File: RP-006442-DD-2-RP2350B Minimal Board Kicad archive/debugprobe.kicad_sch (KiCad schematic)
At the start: 39 parts, among them J4 Conn_01x03, J5 USB_C_Receptacle_USB2.0_16P, SW3 SW_Push, SW4 SW_Push, U5 W25Q128JVS, U6 NCP1117-3.3_SOT223, U7 RP2350_60QFN, Y2 ABM8-272-T3

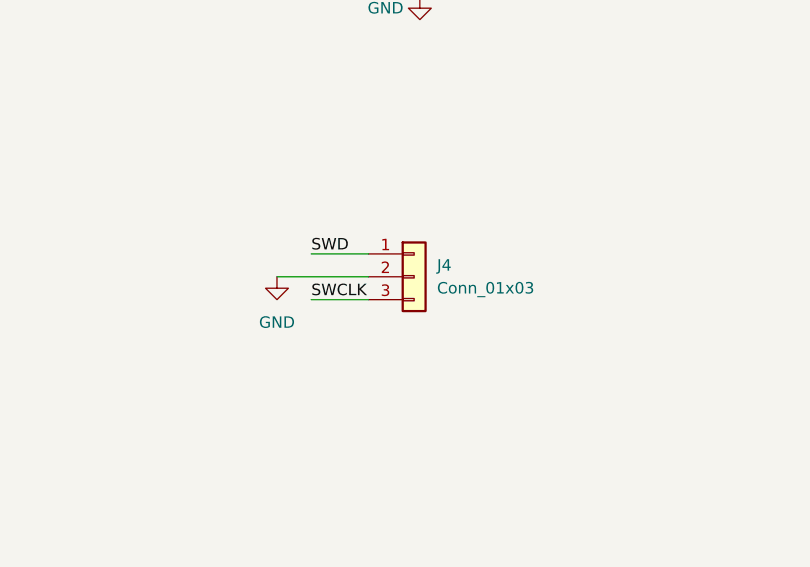
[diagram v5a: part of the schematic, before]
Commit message: Update to schematic and pcb
Changed ht16k33 package from 28SOP to 24SSOP

Placed pcb footprints
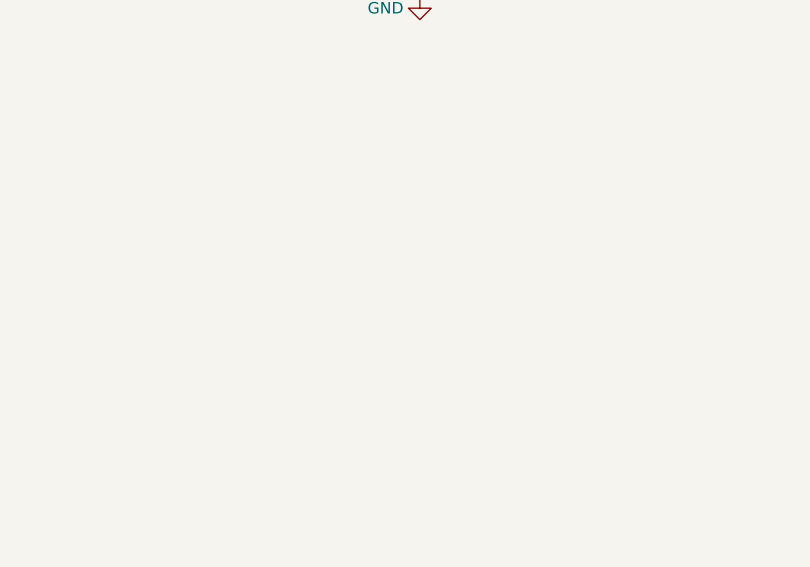
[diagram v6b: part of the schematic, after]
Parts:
- removed J4: Conn_01x03, Connector_PinHeader_2.54mm:PinHeader_1x03_P2.54mm_Vertical, symbol Connector_Generic:Conn_01x03
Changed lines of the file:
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@@
 	(wire
 		(pts
-			(xy 292.1 182.88) (xy 298.45 182.88)
-		)
-		(stroke
-			(width 0)
-			(type default)
-		)
-	)
-	(wire
-		(pts
 			(xy 118.11 49.53) (xy 118.11 50.8)
 		)
@@
 	(wire
 		(pts
-			(xy 292.1 177.8) (xy 298.45 177.8)
-		)
-		(stroke
-			(width 0)
-			(type default)
-		)
-	)
-	(wire
-		(pts
 			(xy 151.13 167.64) (xy 172.72 167.64)
 		)
@@
 	(wire
 		(pts
-			(xy 288.29 180.34) (xy 298.45 180.34)
-		)
-		(stroke
-			(width 0)
-			(type default)
-		)
-	)
-	(wire
-		(pts
 			(xy 236.22 149.86) (xy 251.46 149.86)
 		)
@@
 		)
 	)
-	(label "SWD"
-		(at 292.1 177.8 0)
-		(effects
-			(font
-				(size 1.27 1.27)
-			)
-			(justify left bottom)
-		)
-	)
 	(label "GPIO5"
 		(at 251.46 127 180)
@@
 		)
 	)
-	(label "SWCLK"
-		(at 292.1 182.88 0)
-		(effects
-			(font
-				(size 1.27 1.27)
-			)
-			(justify left bottom)
-		)
-	)
 	(label "SWD"
 		(at 163.83 181.61 0)
@@
 	)
 	(symbol
-		(lib_name "GND_1")
-		(lib_id "power:GND")
-		(at 288.29 180.34 0)
-		(unit 1)
-		(exclude_from_sim no)
-		(in_bom yes)
-		(on_board yes)
-		(dnp no)
-		(fields_autoplaced yes)
-		(property "Reference" "#PWR032"
-			(at 288.29 186.69 0)
-			(effects
-				(font
-					(size 1.27 1.27)
-				)
-				(hide yes)
-			)
-		)
-		(property "Value" "GND"
-			(at 288.29 185.42 0)
-			(effects
-				(font
-					(size 1.27 1.27)
-				)
-			)
-		)
-		(property "Footprint" ""
-			(at 288.29 180.34 0)
-			(effects
-				(font
-					(size 1.27 1.27)
-				)
-				(hide yes)
-			)
-		)
-		(property "Datasheet" ""
-			(at 288.29 180.34 0)
-			(effects
-				(font
-					(size 1.27 1.27)
-				)
-				(hide yes)
-			)
-		)
-		(property "Description" "Power symbol creates a global label with name \"GND\" , ground"
-			(at 288.29 180.34 0)
-			(effects
-				(font
-					(size 1.27 1.27)
-				)
-				(hide yes)
-			)
-		)
-		(pin "1"
-		)
-		(instances
-			(project ""
-				(path "/94683f5c-9cd9-448e-be96-9792537b5cb8/500e1af8-c8c5-44c6-9fbe-f4d5e5ab4ca8"
-					(reference "#PWR032")
-					(unit 1)
-				)
-			)
-		)
-	)
-	(symbol
 		(lib_id "power:GND")
 		(at 78.74 168.91 0)
@@
 					(unit 1)
 				)
-			)
-		)
-	)
-	(symbol
-		(lib_id "Connector_Generic:Conn_01x03")
-		(at 303.53 180.34 0)
-		(unit 1)
-		(exclude_from_sim no)
-		(in_bom yes)
-		(on_board yes)
-		(dnp no)
-		(fields_autoplaced yes)
-		(property "Reference" "J4"
-			(at 306.07 179.0699 0)
-			(effects
-				(font
-					(size 1.27 1.27)
-				)
-				(justify left)
-			)
-		)
-		(property "Value" "Conn_01x03"
-			(at 306.07 181.6099 0)
-			(effects
-				(font
-					(size 1.27 1.27)
-				)
-				(justify left)
-			)
-		)
-		(property "Footprint" "Connector_PinHeader_2.54mm:PinHeader_1x03_P2.54mm_Vertical"
-			(at 303.53 180.34 0)
-			(effects
-				(font
-					(size 1.27 1.27)
-				)
-				(hide yes)
-			)
-		)
-		(property "Datasheet" "~"
-			(at 303.53 180.34 0)
-			(effects
-				(font
-					(size 1.27 1.27)
-				)
-				(hide yes)
-			)
-		)
-		(property "Description" "Generic connector, single row, 01x03, script generated (kicad-library-utils/schlib/autogen/connector/)"
-			(at 303.53 180.34 0)
-			(effects
-				(font
-					(size 1.27 1.27)
-				)
-				(hide yes)
-			)
-		)
-		(pin "2"
-		)
-		(pin "3"
-		)
-		(pin "1"
-		)
-		(instances
-			(project ""
-				(path "/94683f5c-9cd9-448e-be96-9792537b5cb8/500e1af8-c8c5-44c6-9fbe-f4d5e5ab4ca8"
-					(reference "J4")
-					(unit 1)
-				)

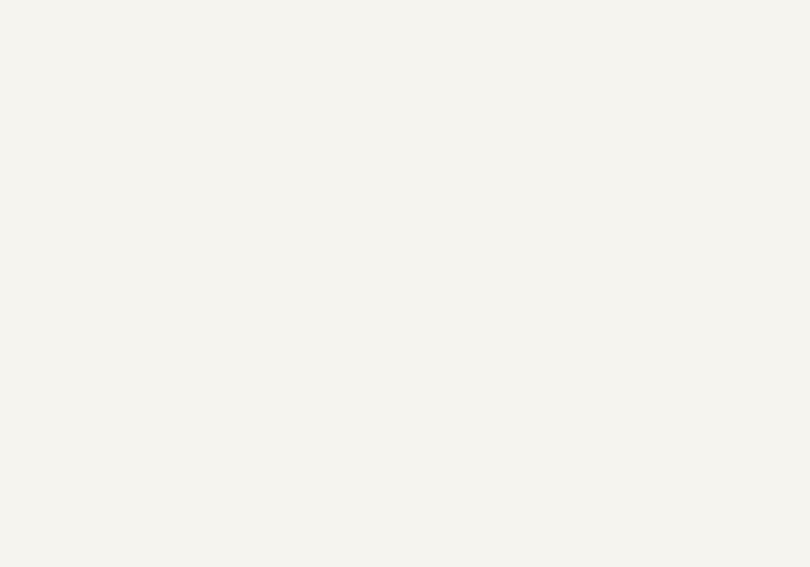
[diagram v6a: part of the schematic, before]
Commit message: Update
fixed some errors in electrical rules checker
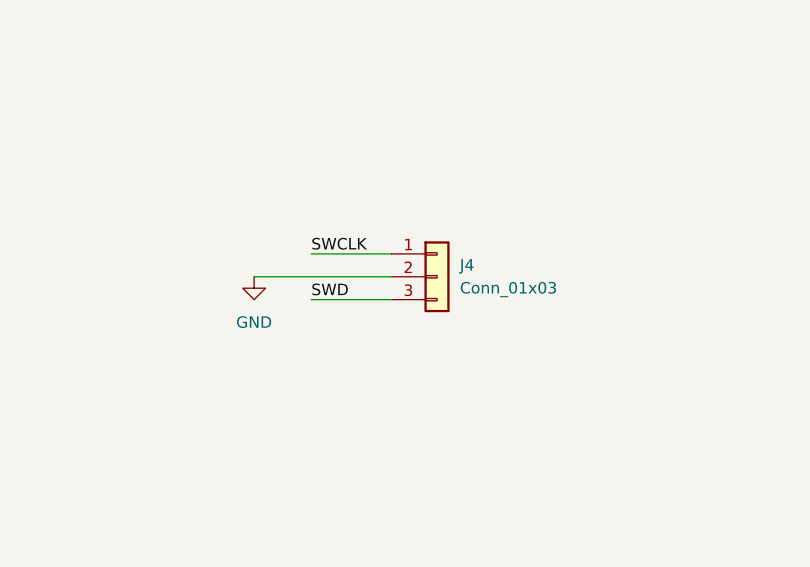
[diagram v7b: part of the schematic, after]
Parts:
- added J4: Conn_01x03, Connector_PinHeader_2.54mm:PinHeader_1x03_P2.54mm_Vertical, symbol Connector_Generic:Conn_01x03
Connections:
- net GND: now also J4.2 (Pin_2)
- net SWCLK: now also J4.1 (Pin_1)
- net SWD: now also J4.3 (Pin_3)
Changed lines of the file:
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@@
 	(wire
 		(pts
+			(xy 294.64 189.23) (xy 309.88 189.23)
+		)
+		(stroke
+			(width 0)
+			(type default)
+		)
+	)
+	(wire
+		(pts
 			(xy 63.5 55.88) (xy 52.07 55.88)
 		)
@@
 	(wire
 		(pts
+			(xy 300.99 186.69) (xy 309.88 186.69)
+		)
+		(stroke
+			(width 0)
+			(type default)
+		)
+	)
+	(wire
+		(pts
 			(xy 181.61 62.23) (xy 181.61 63.5)
 		)
@@
 	(wire
 		(pts
+			(xy 300.99 191.77) (xy 309.88 191.77)
+		)
+		(stroke
+			(width 0)
+			(type default)
+		)
+	)
+	(wire
+		(pts
 			(xy 72.39 158.75) (xy 72.39 162.56)
 		)
@@
 		)
 	)
+	(label "SWCLK"
+		(at 300.99 186.69 0)
+		(effects
+			(font
+				(size 1.27 1.27)
+			)
+			(justify left bottom)
+		)
+	)
 	(label "VREG_AVDD"
 		(at 160.655 92.71 0)
@@
 		)
 	)
+	(label "SWD"
+		(at 300.99 191.77 0)
+		(effects
+			(font
+				(size 1.27 1.27)
+			)
+			(justify left bottom)
+		)
+	)
 	(label "GPIO26_ADC0"
 		(at 251.46 182.88 180)
@@
 	)
 	(symbol
+		(lib_id "Connector_Generic:Conn_01x03")
+		(at 314.96 189.23 0)
+		(unit 1)
+		(exclude_from_sim no)
+		(in_bom yes)
+		(on_board yes)
+		(dnp no)
+		(fields_autoplaced yes)
+		(property "Reference" "J4"
+			(at 317.5 187.9599 0)
+			(effects
+				(font
+					(size 1.27 1.27)
+				)
+				(justify left)
+			)
+		)
+		(property "Value" "Conn_01x03"
+			(at 317.5 190.4999 0)
+			(effects
+				(font
+					(size 1.27 1.27)
+				)
+				(justify left)
+			)
+		)
+		(property "Footprint" "Connector_PinHeader_2.54mm:PinHeader_1x03_P2.54mm_Vertical"
+			(at 314.96 189.23 0)
+			(effects
+				(font
+					(size 1.27 1.27)
+				)
+				(hide yes)
+			)
+		)
+		(property "Datasheet" "~"
+			(at 314.96 189.23 0)
+			(effects
+				(font
+					(size 1.27 1.27)
+				)
+				(hide yes)
+			)
+		)
+		(property "Description" "Generic connector, single row, 01x03, script generated (kicad-library-utils/schlib/autogen/connector/)"
+			(at 314.96 189.23 0)
+			(effects
+				(font
+					(size 1.27 1.27)
+				)
+				(hide yes)
+			)
+		)
+		(pin "2"
+		)
+		(pin "1"
+		)
+		(pin "3"
+		)
+		(instances
+			(project ""
+				(path "/94683f5c-9cd9-448e-be96-9792537b5cb8/500e1af8-c8c5-44c6-9fbe-f4d5e5ab4ca8"
+					(reference "J4")
+					(unit 1)
+				)
+			)
+		)
+	)
+	(symbol
 		(lib_id "power:GND")
 		(at 29.21 81.28 0)
@@
 					(unit 1)
 				)
+			)
+		)
+	)
+	(symbol
+		(lib_name "GND_1")
+		(lib_id "power:GND")
+		(at 294.64 189.23 0)
+		(unit 1)
+		(exclude_from_sim no)
+		(in_bom yes)
+		(on_board yes)
+		(dnp no)
+		(fields_autoplaced yes)
+		(property "Reference" "#PWR067"
+			(at 294.64 195.58 0)
+			(effects
+				(font
+					(size 1.27 1.27)
+				)
+				(hide yes)
+			)
+		)
+		(property "Value" "GND"
+			(at 294.64 194.31 0)
+			(effects
+				(font
+					(size 1.27 1.27)
+				)
+			)
+		)
+		(property "Footprint" ""
+			(at 294.64 189.23 0)
+			(effects
+				(font
+					(size 1.27 1.27)
+				)
+				(hide yes)
+			)
+		)
+		(property "Datasheet" ""
+			(at 294.64 189.23 0)
+			(effects
+				(font
+					(size 1.27 1.27)
+				)
+				(hide yes)
+			)
+		)
+		(property "Description" "Power symbol creates a global label with name \"GND\" , ground"
+			(at 294.64 189.23 0)
+			(effects
+				(font
+					(size 1.27 1.27)
+				)
+				(hide yes)
+			)
+		)
+		(pin "1"
+		)
+		(instances
+			(project ""
+				(path "/94683f5c-9cd9-448e-be96-9792537b5cb8/500e1af8-c8c5-44c6-9fbe-f4d5e5ab4ca8"
+					(reference "#PWR067")
+					(unit 1)
+				)

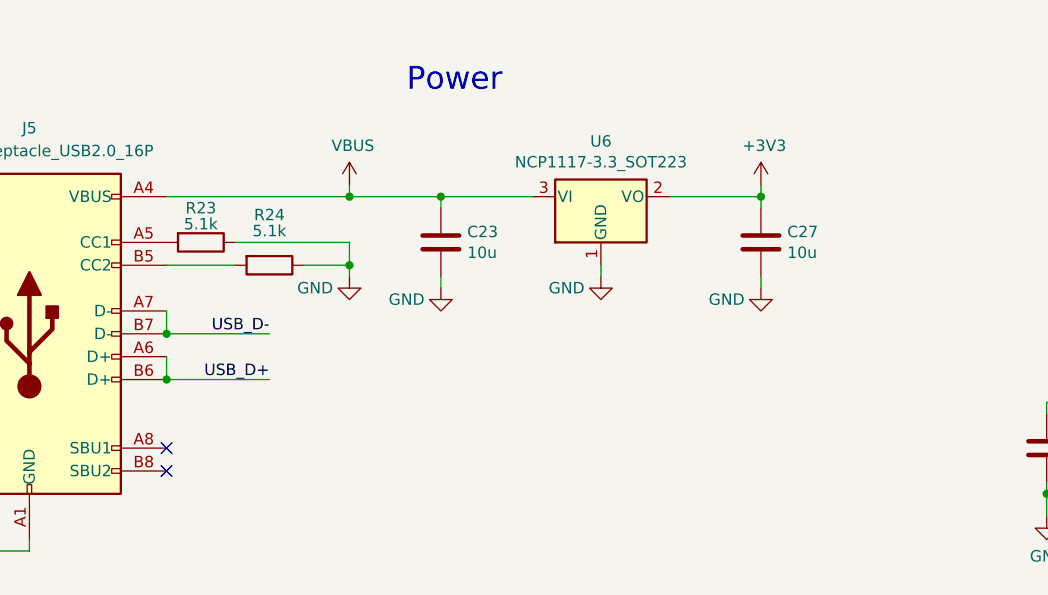
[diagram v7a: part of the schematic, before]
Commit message: Update schematic
added schottky diode to vbus on microcontroller and debug probe
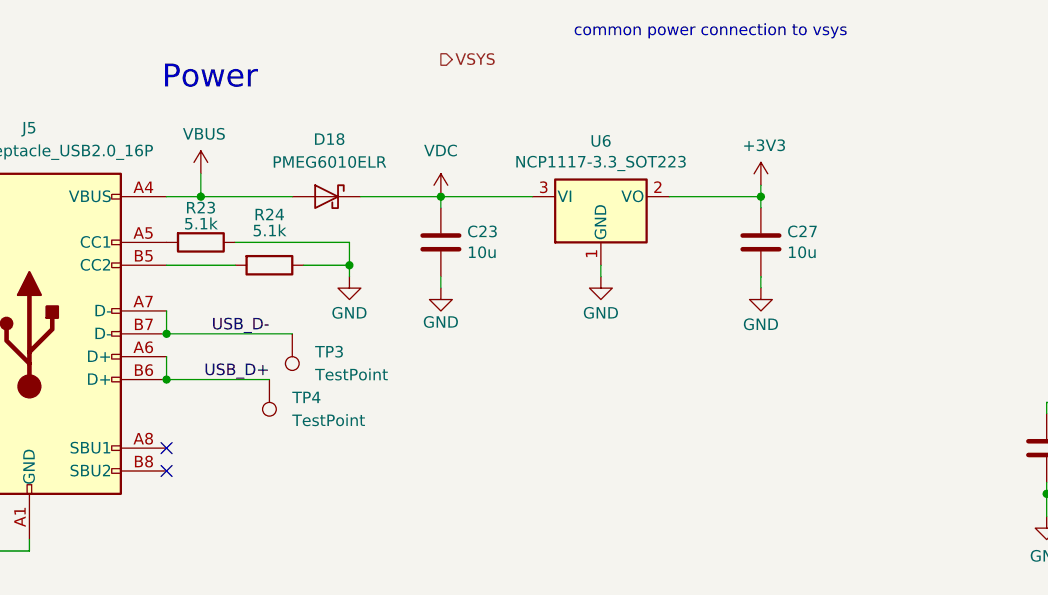
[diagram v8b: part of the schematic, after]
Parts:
- added D18: PMEG6010ELR, Diode_SMD:Nexperia_CFP3_SOD-123W, symbol Diode:PMEG6010ELR
- added TP3, TP4: TestPoint, TestPoint:TestPoint_Pad_2.0x2.0mm, symbol Connector:TestPoint
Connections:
- net USB_D+: now also TP4.1
- net USB_D-: now also TP3.1
- net VBUS: now also D18.2 (A); no longer C23.1, U6.3 (VI)
- new net VDC: C23.1, D18.1 (K), U6.3 (VI)
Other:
- note added: "common power connection to vsys"
